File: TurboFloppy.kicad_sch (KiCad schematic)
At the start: 10 parts, among them CN1 EXPANSION_PORT, CN3 PIN_HEADER_32PIN, U1 8255, U2 GAL20V8

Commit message: (Very) Final touches Note project URL is still missing!
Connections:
- net a10: now also U2.6 (I6); no longer U2.5 (I5)
- net a11: now also U2.5 (I5); no longer U2.20 (I020)
- net a5: now also U2.15 (IO15); no longer U2.9 (I9)
- net a6: now also U2.9 (I9); no longer U2.8 (I8)
- net a7: now also U2.16 (IO16); no longer U2.7 (I7)
- net a8: now also U2.8 (I8); no longer U2.6 (I6)
- net a9: now also U2.7 (I7); no longer U2.19 (IO19)
- net reset: now also U2.17 (IO17); no longer U2.15 (IO15)
- net ~{cs8255}: now also U2.20 (I020); no longer U2.18 (IO18)
- net ~{rd8255}: now also U2.19 (IO19); no longer U2.17 (IO17)
- net ~{wr8255}: now also U2.18 (IO18); no longer U2.16 (IO16)
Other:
- note removed: "rd = !(phi2 & aec & rw & ba) wr = !(phi2 & aec & !rw)"

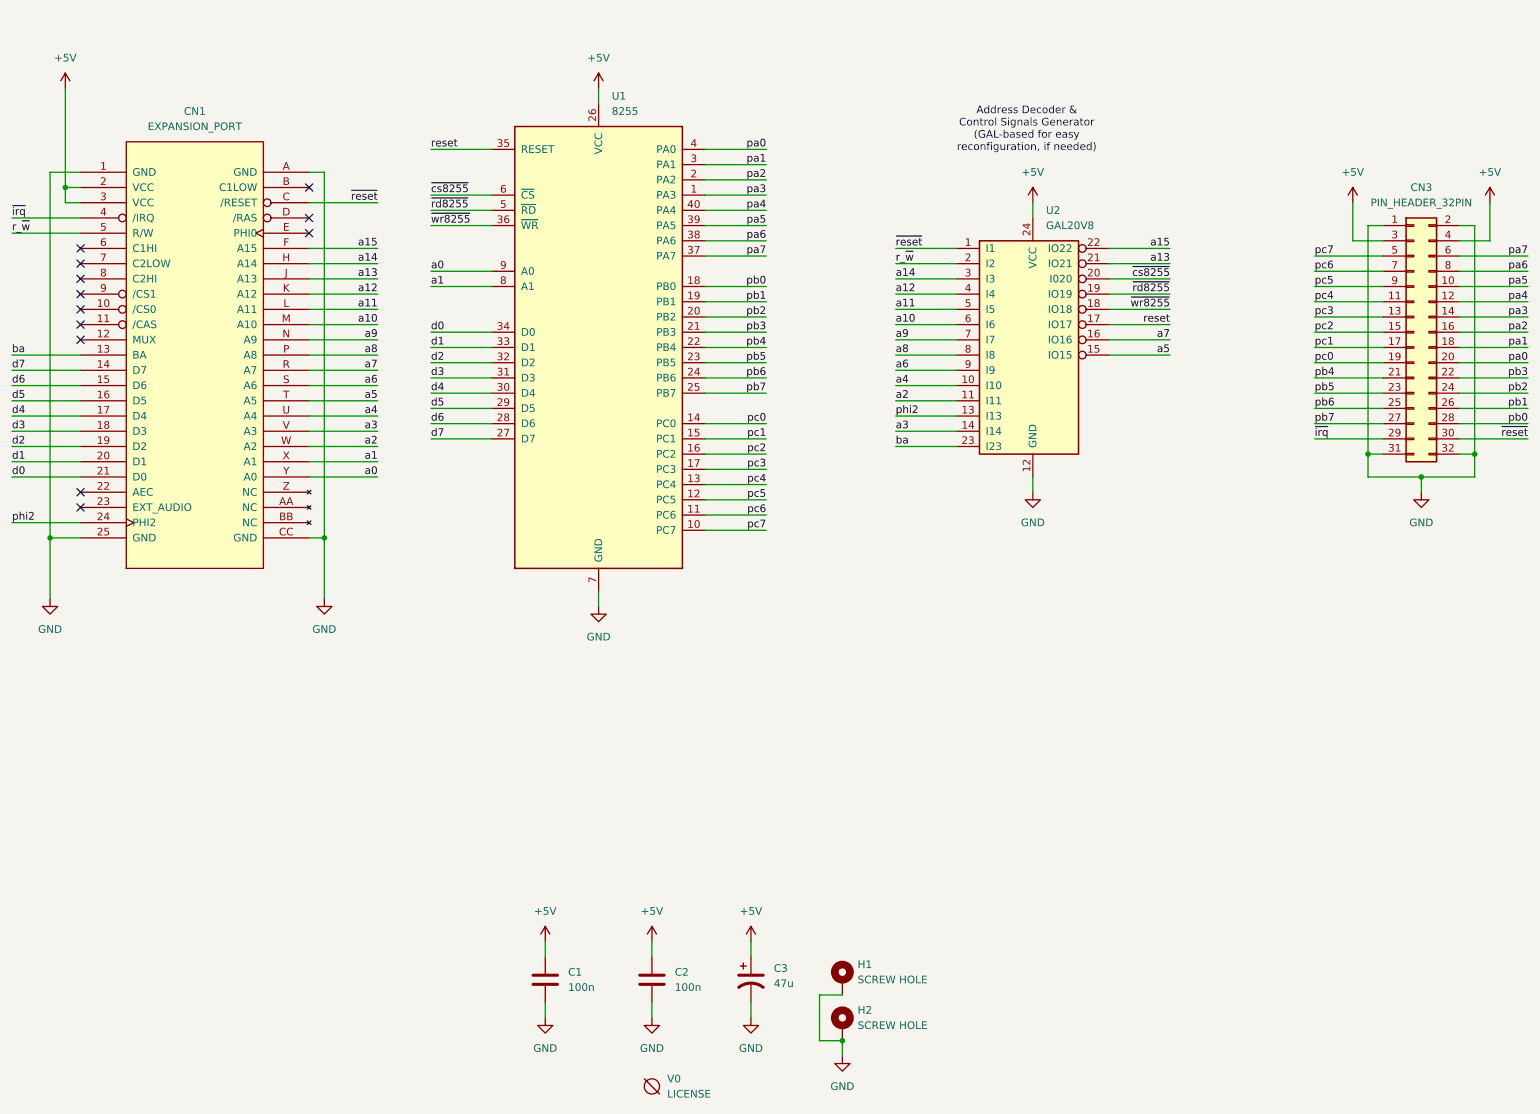
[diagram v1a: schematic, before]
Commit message: Add pull-ups on all 8255 ports
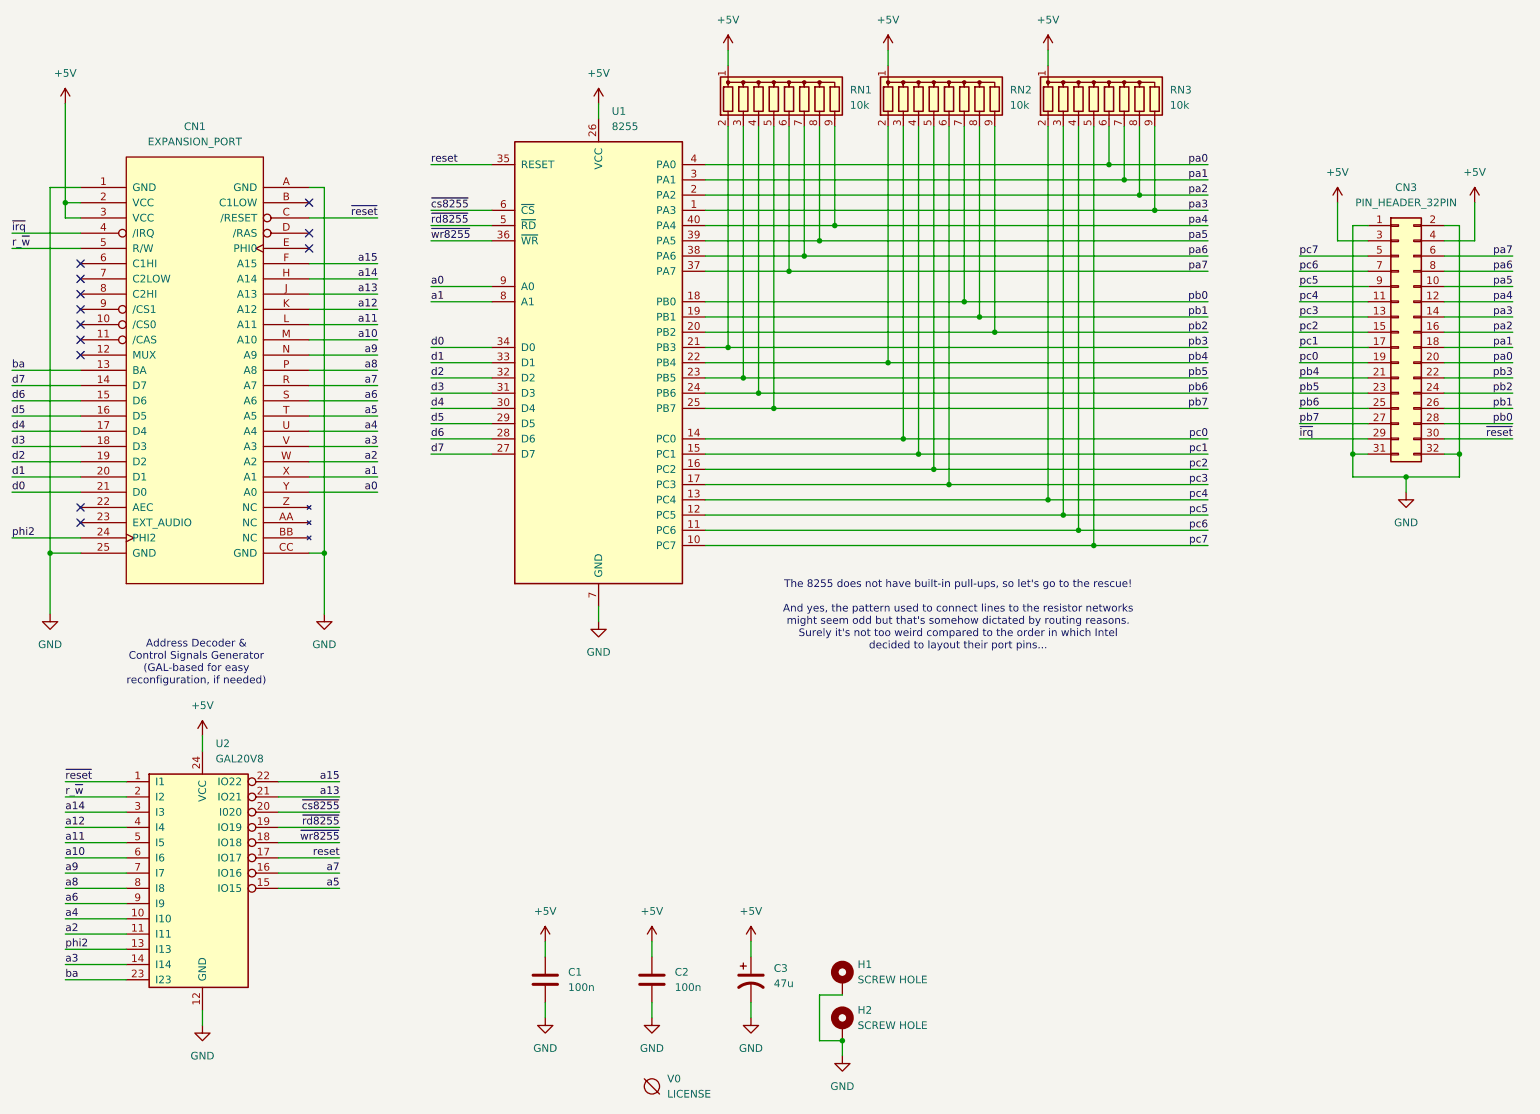
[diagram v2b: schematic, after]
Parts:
- added RN1, RN2, RN3: 10k, Resistor_THT:R_Array_SIP9, symbol Device:R_Network08
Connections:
- net +5V: now also RN1.1 (common), RN2.1 (common), RN3.1 (common)
- net pa0: now also RN3.6 (R5)
- net pa1: now also RN3.7 (R6)
- net pa2: now also RN3.8 (R7)
- net pa3: now also RN3.9 (R8)
- net pa4: now also RN1.9 (R8)
- net pa5: now also RN1.8 (R7)
- net pa6: now also RN1.7 (R6)
- net pa7: now also RN1.6 (R5)
- net pb0: now also RN2.7 (R6)
- net pb1: now also RN2.8 (R7)
- net pb2: now also RN2.9 (R8)
- net pb3: now also RN1.2 (R1)
- net pb4: now also RN2.2 (R1)
- net pb5: now also RN1.3 (R2)
- net pb6: now also RN1.4 (R3)
- net pb7: now also RN1.5 (R4)
- net pc0: now also RN2.3 (R2)
- net pc1: now also RN2.4 (R3)
- net pc2: now also RN2.5 (R4)
- net pc3: now also RN2.6 (R5)
- net pc4: now also RN3.2 (R1)
- net pc5: now also RN3.3 (R2)
- net pc6: now also RN3.4 (R3)
- net pc7: now also RN3.5 (R4)
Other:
- note added: "The 8255 does not have built-in pull-ups, so let's go to the rescue! And yes, the pattern used to connect lines to the resistor networks might seem odd but that's somehow dictated by routing reasons. Surely it's not too weird compared to the order in which Intel decided to layout their port pins..."
- moved on the sheet: CN1, CN3, U1, U2

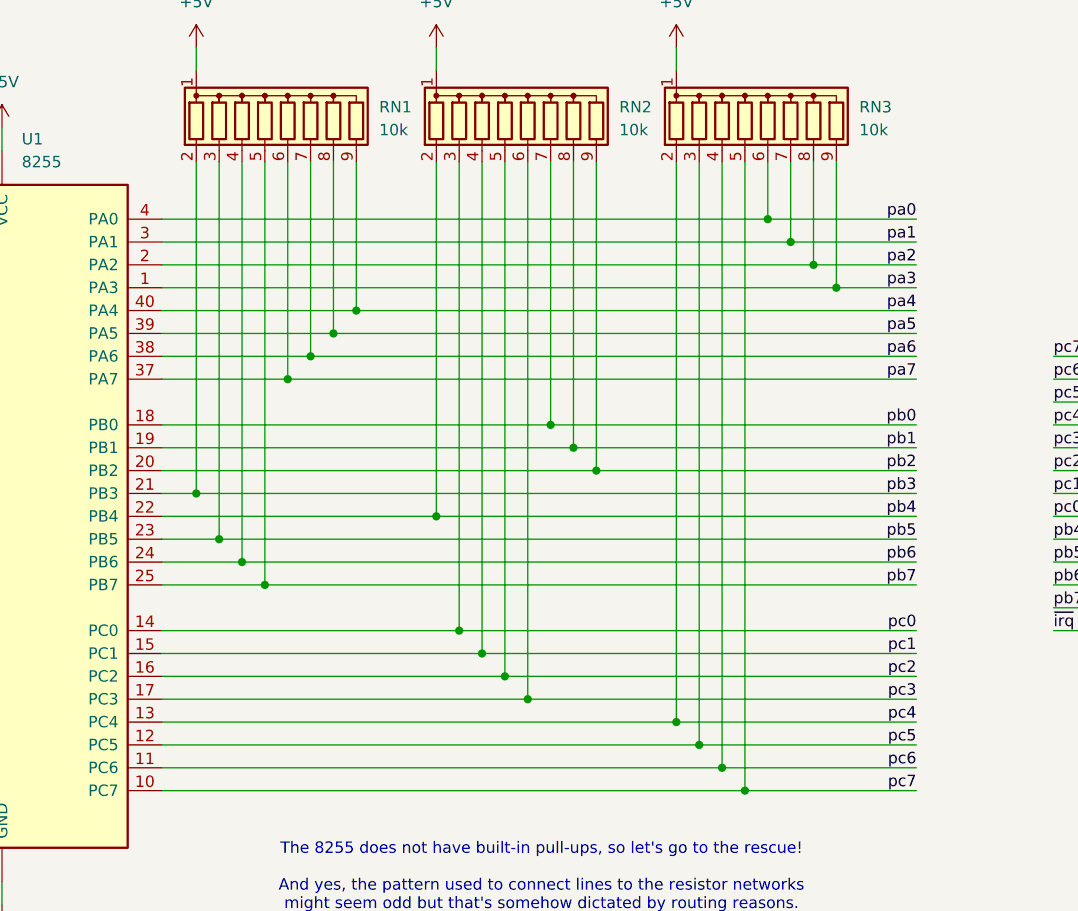
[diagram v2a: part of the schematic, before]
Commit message: Rework some tracks
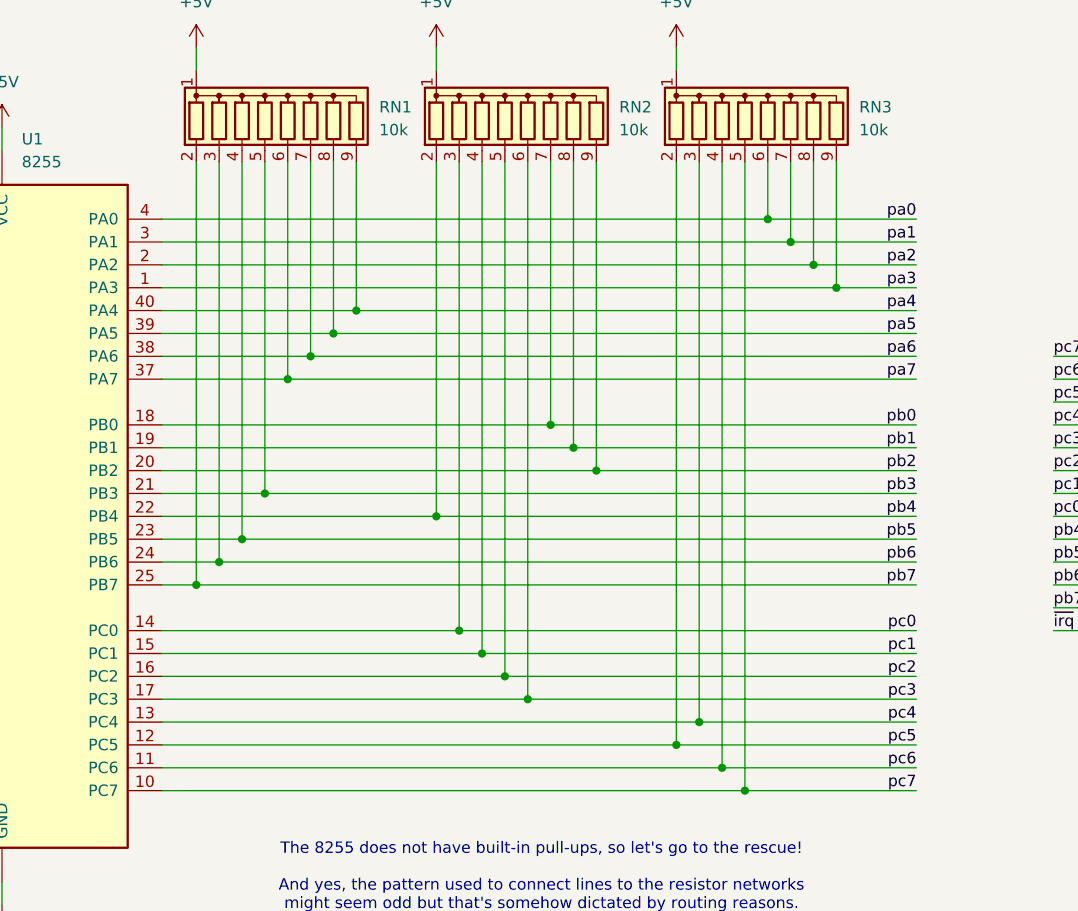
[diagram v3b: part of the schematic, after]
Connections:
- net pb3: now also RN1.5 (R4); no longer RN1.2 (R1)
- net pb5: now also RN1.4 (R3); no longer RN1.3 (R2)
- net pb6: now also RN1.3 (R2); no longer RN1.4 (R3)
- net pb7: now also RN1.2 (R1); no longer RN1.5 (R4)
- net pc4: now also RN3.3 (R2); no longer RN3.2 (R1)
- net pc5: now also RN3.2 (R1); no longer RN3.3 (R2)
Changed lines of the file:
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@@
-	)
-	(junction
-		(at 148.59 80.01)
-		(diameter 0)
-		(color 0 0 0 0)
 	)
 	(junction
@@
 	)
 	(junction
-		(at 194.31 95.25)
+		(at 194.31 97.79)
 		(diameter 0)
 		(color 0 0 0 0)
@@
 	)
 	(junction
+		(at 148.59 69.85)
+		(diameter 0)
+		(color 0 0 0 0)
+	)
+	(junction
+		(at 140.97 80.01)
+		(diameter 0)
+		(color 0 0 0 0)
+	)
+	(junction
 		(at 27.94 104.14)
 		(diameter 0)
@@
 	)
 	(junction
-		(at 146.05 77.47)
+		(at 196.85 95.25)
 		(diameter 0)
 		(color 0 0 0 0)
@@
 	)
 	(junction
+		(at 146.05 74.93)
+		(diameter 0)
+		(color 0 0 0 0)
+	)
+	(junction
 		(at 254 91.44)
 		(diameter 0)
@@
 	)
 	(junction
-		(at 143.51 74.93)
-		(diameter 0)
-		(color 0 0 0 0)
-	)
-	(junction
 		(at 209.55 44.45)
 		(diameter 0)
@@
 	)
 	(junction
-		(at 196.85 97.79)
-		(diameter 0)
-		(color 0 0 0 0)
-	)
-	(junction
 		(at 180.34 62.23)
 		(diameter 0)
@@
 	)
 	(junction
-		(at 140.97 69.85)
-		(diameter 0)
-		(color 0 0 0 0)
-	)
-	(junction
 		(at 245.11 87.63)
 		(diameter 0)
@@
 	(junction
 		(at 175.26 90.17)
+		(diameter 0)
+		(color 0 0 0 0)
+	)
+	(junction
+		(at 143.51 77.47)
 		(diameter 0)
 		(color 0 0 0 0)
@@
 	(wire
 		(pts
-			(xy 148.59 80.01) (xy 220.98 80.01)
-		)
-		(stroke
-			(width 0)
-			(type default)
-		)
-	)
-	(wire
-		(pts
 			(xy 167.64 33.02) (xy 167.64 72.39)
 		)
@@
 	(wire
 		(pts
-			(xy 137.16 69.85) (xy 140.97 69.85)
-		)
-		(stroke
-			(width 0)
-			(type default)
-		)
-	)
-	(wire
-		(pts
 			(xy 30.48 45.72) (xy 30.48 48.26)
 		)
@@
 	(wire
 		(pts
-			(xy 143.51 33.02) (xy 143.51 74.93)
-		)
-		(stroke
-			(width 0)
-			(type default)
-		)
-	)
-	(wire
-		(pts
 			(xy 71.12 104.14) (xy 73.66 104.14)
 		)
@@
 	(wire
 		(pts
+			(xy 143.51 77.47) (xy 220.98 77.47)
+		)
+		(stroke
+			(width 0)
+			(type default)
+		)
+	)
+	(wire
+		(pts
 			(xy 156.21 177.8) (xy 156.21 185.42)
 		)
@@
 	(wire
 		(pts
+			(xy 148.59 69.85) (xy 220.98 69.85)
+		)
+		(stroke
+			(width 0)
+			(type default)
+		)
+	)
+	(wire
+		(pts
 			(xy 30.48 45.72) (xy 33.02 45.72)
 		)
@@
 	(wire
 		(pts
-			(xy 137.16 97.79) (xy 196.85 97.79)
+			(xy 137.16 97.79) (xy 194.31 97.79)
 		)
 		(stroke
@@
 	(wire
 		(pts
+			(xy 194.31 33.02) (xy 194.31 97.79)
+		)
+		(stroke
+			(width 0)
+			(type default)
+		)
+	)
+	(wire
+		(pts
 			(xy 153.67 54.61) (xy 220.98 54.61)
 		)
@@
 	(wire
 		(pts
-			(xy 196.85 33.02) (xy 196.85 97.79)
+			(xy 196.85 33.02) (xy 196.85 95.25)
 		)
 		(stroke
@@
 	(wire
 		(pts
-			(xy 137.16 80.01) (xy 148.59 80.01)
+			(xy 137.16 80.01) (xy 140.97 80.01)
 		)
 		(stroke
@@
 	(wire
 		(pts
-			(xy 137.16 77.47) (xy 146.05 77.47)
-		)
-		(stroke
-			(width 0)
-			(type default)
-		)
-	)
-	(wire
-		(pts
 			(xy 212.09 33.02) (xy 212.09 46.99)
 		)
@@
 	(wire
 		(pts
+			(xy 140.97 33.02) (xy 140.97 80.01)
+		)
+		(stroke
+			(width 0)
+			(type default)
+		)
+	)
+	(wire
+		(pts
 			(xy 40.64 162.56) (xy 30.48 162.56)
 		)
@@
 	(wire
 		(pts
-			(xy 140.97 33.02) (xy 140.97 69.85)
-		)
-		(stroke
-			(width 0)
-			(type default)
-		)
-	)
-	(wire
-		(pts
 			(xy 40.64 157.48) (xy 30.48 157.48)
 		)
@@
 	(wire
 		(pts
-			(xy 196.85 97.79) (xy 220.98 97.79)
+			(xy 194.31 97.79) (xy 220.98 97.79)
 		)
 		(stroke
@@
 	(wire
 		(pts
+			(xy 148.59 33.02) (xy 148.59 69.85)
+		)
+		(stroke
+			(width 0)
+			(type default)
+		)
+	)
+	(wire
+		(pts
 			(xy 53.34 180.34) (xy 53.34 182.88)
 		)
@@
 	(wire
 		(pts
-			(xy 137.16 95.25) (xy 194.31 95.25)
-		)
-		(stroke
-			(width 0)
-			(type default)
-		)
-	)
-	(wire
-		(pts
 			(xy 137.16 102.87) (xy 201.93 102.87)
 		)
@@
 	(wire
 		(pts
+			(xy 196.85 95.25) (xy 220.98 95.25)
+		)
+		(stroke
+			(width 0)
+			(type default)
+		)
+	)
+	(wire
+		(pts
 			(xy 137.16 64.77) (xy 182.88 64.77)
 		)
@@
 	(wire
 		(pts
-			(xy 137.16 74.93) (xy 143.51 74.93)
-		)
-		(stroke
-			(width 0)
-			(type default)
-		)
-	)
-	(wire
-		(pts
-			(xy 148.59 33.02) (xy 148.59 80.01)
-		)
-		(stroke
-			(width 0)
-			(type default)
-		)
-	)
-	(wire
-		(pts
 			(xy 236.22 67.31) (xy 247.65 67.31)
 		)
@@
 	(wire
 		(pts
-			(xy 194.31 33.02) (xy 194.31 95.25)
+			(xy 140.97 80.01) (xy 220.98 80.01)
 		)
 		(stroke
@@
 	(wire
 		(pts
-			(xy 194.31 95.25) (xy 220.98 95.25)
+			(xy 137.16 95.25) (xy 196.85 95.25)
 		)
 		(stroke
@@
 	(wire
 		(pts
-			(xy 146.05 33.02) (xy 146.05 77.47)
-		)
-		(stroke
-			(width 0)
-			(type default)
-		)
-	)
-	(wire
-		(pts
 			(xy 144.78 168.91) (xy 144.78 171.45)
 		)
@@
 	(wire
 		(pts
-			(xy 140.97 69.85) (xy 220.98 69.85)
+			(xy 137.16 69.85) (xy 148.59 69.85)
 		)
 		(stroke
@@
 	(wire
 		(pts
+			(xy 143.51 33.02) (xy 143.51 77.47)
+		)
+		(stroke
+			(width 0)
+			(type default)
+		)
+	)
+	(wire
+		(pts
 			(xy 40.64 149.86) (xy 30.48 149.86)
 		)
@@
 	(wire
 		(pts
-			(xy 143.51 74.93) (xy 220.98 74.93)
+			(xy 137.16 74.93) (xy 146.05 74.93)
 		)
 		(stroke
@@
 	(wire
 		(pts
+			(xy 146.05 74.93) (xy 220.98 74.93)
+		)
+		(stroke
+			(width 0)
+			(type default)
+		)
+	)
+	(wire
+		(pts
 			(xy 101.6 77.47) (xy 91.44 77.47)
 		)
@@
 	(wire
 		(pts
+			(xy 146.05 33.02) (xy 146.05 74.93)
+		)
+		(stroke
+			(width 0)
+			(type default)
+		)
+	)
+	(wire
+		(pts
 			(xy 101.6 87.63) (xy 91.44 87.63)
 		)
@@
 	(wire
 		(pts
-			(xy 146.05 77.47) (xy 220.98 77.47)
-		)
-		(stroke
+			(xy 137.16 77.47) (xy 143.51 77.47)
+		)
+		(stroke

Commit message: Minor tweaks + Add URL
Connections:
- net pb3: now also RN2.2 (R1); no longer RN1.5 (R4)
- net pb4: now also RN1.5 (R4); no longer RN2.2 (R1)
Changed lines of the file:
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@@
-	)
-	(junction
-		(at 167.64 72.39)
-		(diameter 0)
-		(color 0 0 0 0)
 	)
 	(junction
@@
 	)
 	(junction
-		(at 148.59 69.85)
+		(at 148.59 72.39)
+		(diameter 0)
+		(color 0 0 0 0)
+	)
+	(junction
+		(at 167.64 69.85)
 		(diameter 0)
 		(color 0 0 0 0)
@@
 	(wire
 		(pts
-			(xy 167.64 33.02) (xy 167.64 72.39)
+			(xy 167.64 33.02) (xy 167.64 69.85)
 		)
 		(stroke
@@
 	(wire
 		(pts
-			(xy 137.16 72.39) (xy 167.64 72.39)
-		)
-		(stroke
-			(width 0)
-			(type default)
-		)
-	)
-	(wire
-		(pts
 			(xy 137.16 92.71) (xy 177.8 92.71)
 		)
@@
 	(wire
 		(pts
+			(xy 148.59 72.39) (xy 220.98 72.39)
+		)
+		(stroke
+			(width 0)
+			(type default)
+		)
+	)
+	(wire
+		(pts
 			(xy 143.51 77.47) (xy 220.98 77.47)
 		)
@@
 	(wire
 		(pts
-			(xy 148.59 69.85) (xy 220.98 69.85)
-		)
-		(stroke
-			(width 0)
-			(type default)
-		)
-	)
-	(wire
-		(pts
 			(xy 30.48 45.72) (xy 33.02 45.72)
 		)
@@
 	(wire
 		(pts
+			(xy 167.64 69.85) (xy 220.98 69.85)
+		)
+		(stroke
+			(width 0)
+			(type default)
+		)
+	)
+	(wire
+		(pts
 			(xy 260.35 62.23) (xy 271.78 62.23)
 		)
@@
 	(wire
 		(pts
-			(xy 148.59 33.02) (xy 148.59 69.85)
+			(xy 148.59 33.02) (xy 148.59 72.39)
 		)
 		(stroke
@@
 	(wire
 		(pts
-			(xy 137.16 69.85) (xy 148.59 69.85)
+			(xy 137.16 69.85) (xy 167.64 69.85)
 		)
 		(stroke
@@
 	(wire
 		(pts
-			(xy 167.64 72.39) (xy 220.98 72.39)
-		)
-		(stroke
+			(xy 137.16 72.39) (xy 148.59 72.39)
+		)
+		(stroke
